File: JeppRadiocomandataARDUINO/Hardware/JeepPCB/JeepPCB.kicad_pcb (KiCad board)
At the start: 2 copper layers, 47.5 x 32.8 mm, 11 parts, among them J1 Conn_01x03_Male

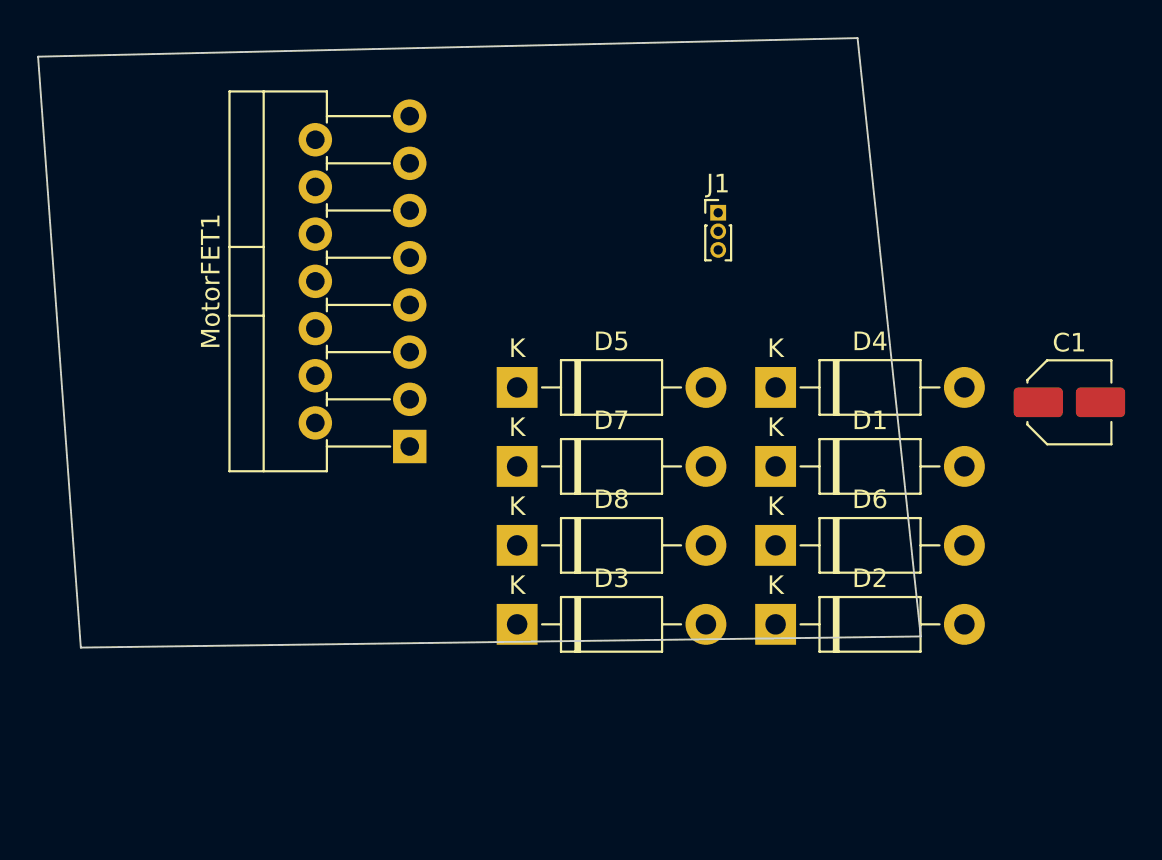
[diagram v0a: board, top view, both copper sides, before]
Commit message: Aggiunta della CPU ATmega328P
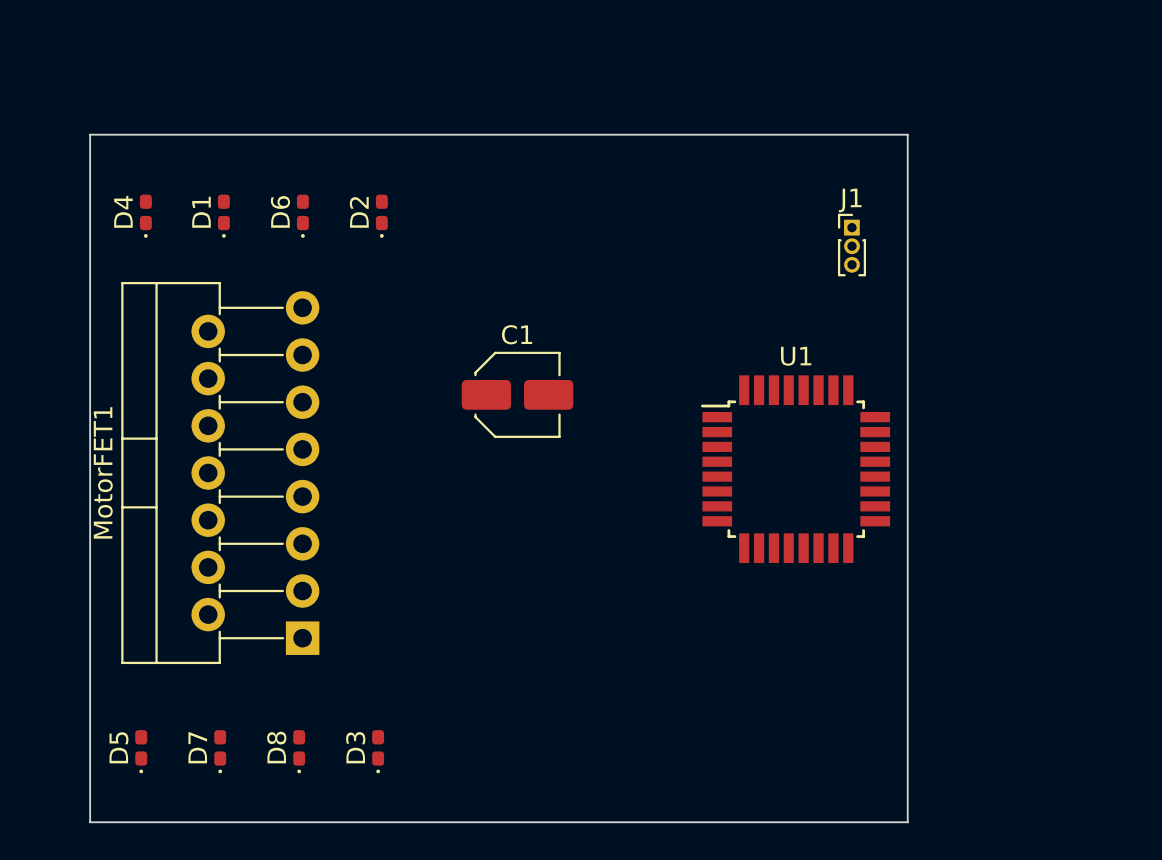
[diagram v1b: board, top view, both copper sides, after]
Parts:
- added U1: ATmega328P-A, Package_QFP:TQFP-32_7x7mm_P0.8mm, F.Cu at (134.0, 77.0)
- D1, D2, D3, D4, D5, D6, D7, D8: footprint Diode_THT:D_DO-41_SOD81_P10.16mm_Horizontal -> Diode_SMD:D_0402_1005Metric_Pad0.77x0.64mm_HandSolder
- J1: value Conn_01x03_Male -> Radio
- moved D4 35.2 mm to (99.0, 63.2), turned to 90 degrees
- moved D1 32.7 mm to (103.2, 63.2), turned to 90 degrees
- moved D6 31.1 mm to (107.5, 63.2), turned to 90 degrees
- moved D2 30.7 mm to (111.7, 63.2), turned to 90 degrees
- moved C1 29.7 mm to (119.0, 73.0)
- moved D5 28.0 mm to (98.8, 92.0), turned to 90 degrees
- moved D7 22.0 mm to (103.0, 92.0), turned to 90 degrees
- moved D8 16.0 mm to (107.2, 92.0), turned to 90 degrees
- moved MotorFET1 11.8 mm to (107.4, 86.1)
- moved D3 10.0 mm to (111.5, 92.0), turned to 90 degrees
- moved J1 7.24 mm to (137.0, 64.0)
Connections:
- J1 pad 1: Net-(J1-Pad1) -> unconnected-(J1-Pad1)
- J1 pad 2: Net-(J1-Pad2) -> unconnected-(J1-Pad2)
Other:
- board size 47.5 x 32.8 mm -> 44 x 37 mm

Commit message: Aggiornamento del PCB
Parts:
- added REG_LIN1: KA78M05_TO252, Package_TO_SOT_SMD:TO-252-2, F.Cu at (114.0, 83.0)
- added C2: 220uF, Capacitor_SMD:C_Elec_4x5.8, F.Cu at (124.0, 78.0)
- added J_BACK1: Screw_Terminal_01x02, TerminalBlock_Phoenix:TerminalBlock_Phoenix_MKDS-1,5-2-5.08_1x02_P5.08mm_Horizontal, F.Cu at (127.5, 59.7)
- added J_FRONT1: Screw_Terminal_01x02, TerminalBlock_Phoenix:TerminalBlock_Phoenix_MKDS-1,5-2-5.08_1x02_P5.08mm_Horizontal, F.Cu at (122.5, 89.3)
- added J_MAIN_POWER1: Screw_Terminal_01x03, TerminalBlock_Phoenix:TerminalBlock_Phoenix_MKDS-1,5-3_1x03_P5.00mm_Horizontal, F.Cu at (137.3, 92.0)
- moved U1 4.00 mm to (134.0, 73.0)
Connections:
- net OUT1 renamed Net-(D1-Pad1)
- net OUT2 renamed Net-(D2-Pad1)
- net OUT3 renamed Net-(D3-Pad1)
- net OUT4 renamed Net-(D4-Pad1)
- J1 pad 1: unconnected-(J1-Pad1) -> Earth
- MotorFET1 pad 10: unconnected-(MotorFET1-Pad10) -> INO_D7
- MotorFET1 pad 11: unconnected-(MotorFET1-Pad11) -> INO_D5
- MotorFET1 pad 12: unconnected-(MotorFET1-Pad12) -> INO_D6
- MotorFET1 pad 5: unconnected-(MotorFET1-Pad5) -> INO_D9
- MotorFET1 pad 6: unconnected-(MotorFET1-Pad6) -> INO_D10
- MotorFET1 pad 7: unconnected-(MotorFET1-Pad7) -> INO_D8
- MotorFET1 pad 9: unconnected-(MotorFET1-Pad9) -> Net-(J_MAIN_POWER1-Pad3)
- U1 pad 21: Net-(U1-Pad21) -> Earth
- U1 pad 3: Net-(U1-Pad21) -> Earth
- U1 pad 5: Net-(U1-Pad21) -> Earth
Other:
- board size 44 x 37 mm -> 48 x 43 mm

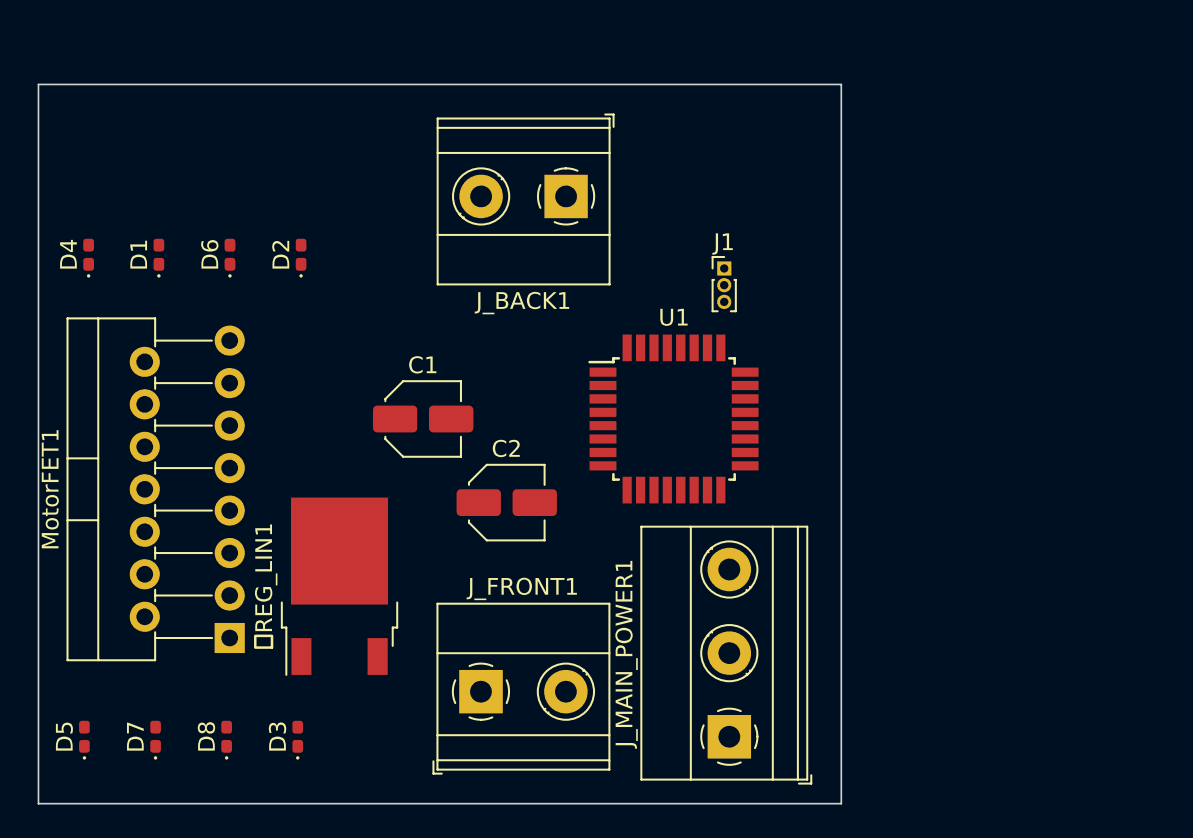
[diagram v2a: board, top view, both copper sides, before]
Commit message: Aggiornamento PCB Jeep
Aggiunta delle connessioni necessarie per il processore
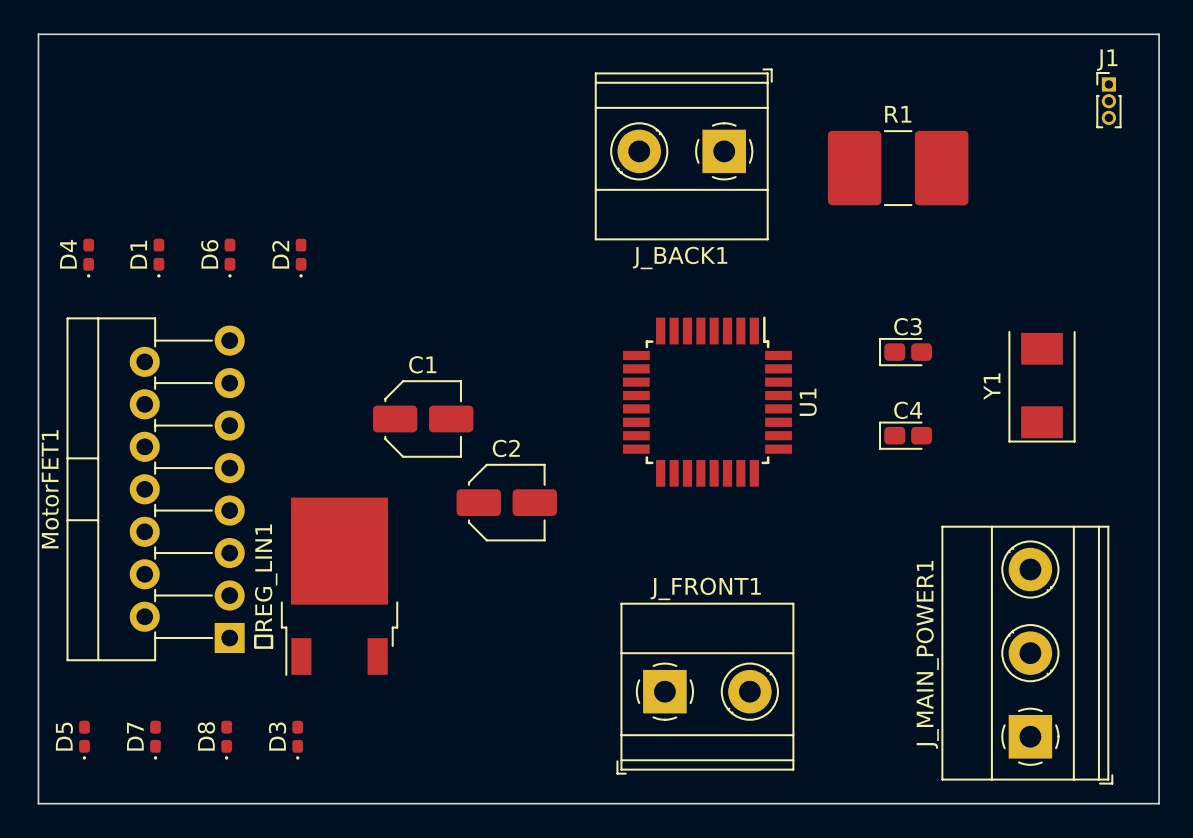
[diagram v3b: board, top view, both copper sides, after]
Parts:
- added C3: 22pF, Capacitor_Tantalum_SMD:CP_EIA-1608-10_AVX-L_Pad1.25x1.05mm_HandSolder, F.Cu at (148.0, 69.0)
- added C4: 22pF, Capacitor_Tantalum_SMD:CP_EIA-1608-10_AVX-L_Pad1.25x1.05mm_HandSolder, F.Cu at (148.0, 74.0)
- added R1: 10K, Resistor_SMD:R_2816_7142Metric_Pad3.20x4.45mm_HandSolder, F.Cu at (147.4, 58.0)
- added Y1: Crystal, Crystal:Crystal_SMD_0603-2Pin_6.0x3.5mm, F.Cu at (156.0, 71.0)
- moved J1 25.5 mm to (160.0, 53.0)
- moved J_MAIN_POWER1 18.0 mm to (155.3, 92.0)
- moved J_FRONT1 11.0 mm to (133.5, 89.3)
- moved J_BACK1 9.83 mm to (137.0, 57.0)
- moved U1 2.24 mm to (136.0, 72.0), turned to -90 degrees
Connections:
- net Net-(C1-Pad1) renamed /5-12V
- REG_LIN1 pad 3: Net-(J_MAIN_POWER1-Pad3) -> VCC
- C2 pad 1: Net-(J_MAIN_POWER1-Pad3) -> VCC
- J1 pad 2: unconnected-(J1-Pad2) -> VCC
- J_MAIN_POWER1 pad 3: Net-(J_MAIN_POWER1-Pad3) -> VCC
- MotorFET1 pad 9: Net-(J_MAIN_POWER1-Pad3) -> VCC
- U1 pad 10: unconnected-(U1-Pad10) -> INO_D6
- U1 pad 11: unconnected-(U1-Pad11) -> INO_D7
- U1 pad 12: unconnected-(U1-Pad12) -> INO_D8
- U1 pad 13: unconnected-(U1-Pad13) -> INO_D9
- U1 pad 14: unconnected-(U1-Pad14) -> INO_D10
- U1 pad 18: unconnected-(U1-Pad18) -> VCC
- U1 pad 20: unconnected-(U1-Pad20) -> VCC
- U1 pad 29: unconnected-(U1-Pad29) -> Net-(R1-Pad2)
- U1 pad 4: Net-(U1-Pad4) -> VCC
- U1 pad 6: Net-(U1-Pad4) -> VCC
- U1 pad 7: unconnected-(U1-Pad7) -> Net-(C3-Pad2)
- U1 pad 8: unconnected-(U1-Pad8) -> Net-(C4-Pad2)
- U1 pad 9: unconnected-(U1-Pad9) -> INO_D5
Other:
- board size 48 x 43 mm -> 67 x 46 mm

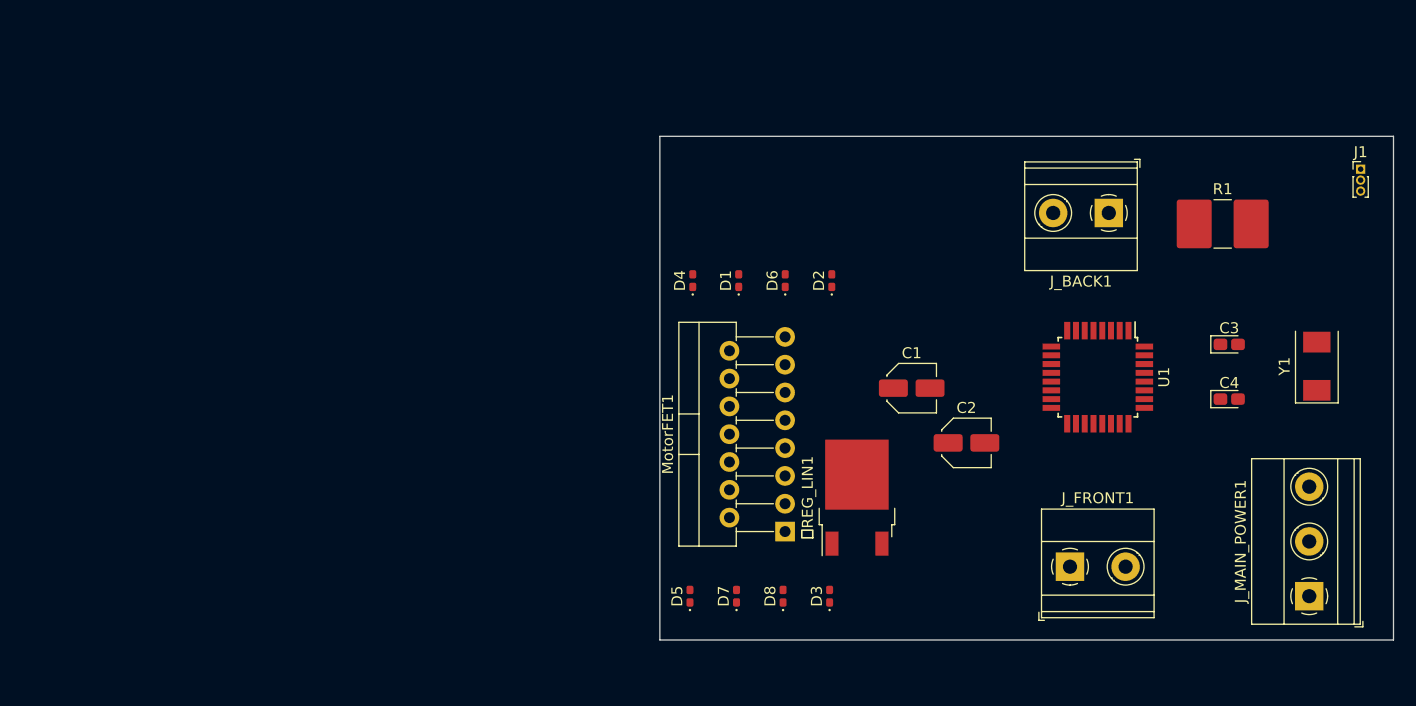
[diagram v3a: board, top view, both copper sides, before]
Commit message: Aggiornamento della resistenza da 10K e posizionamento dei componenti
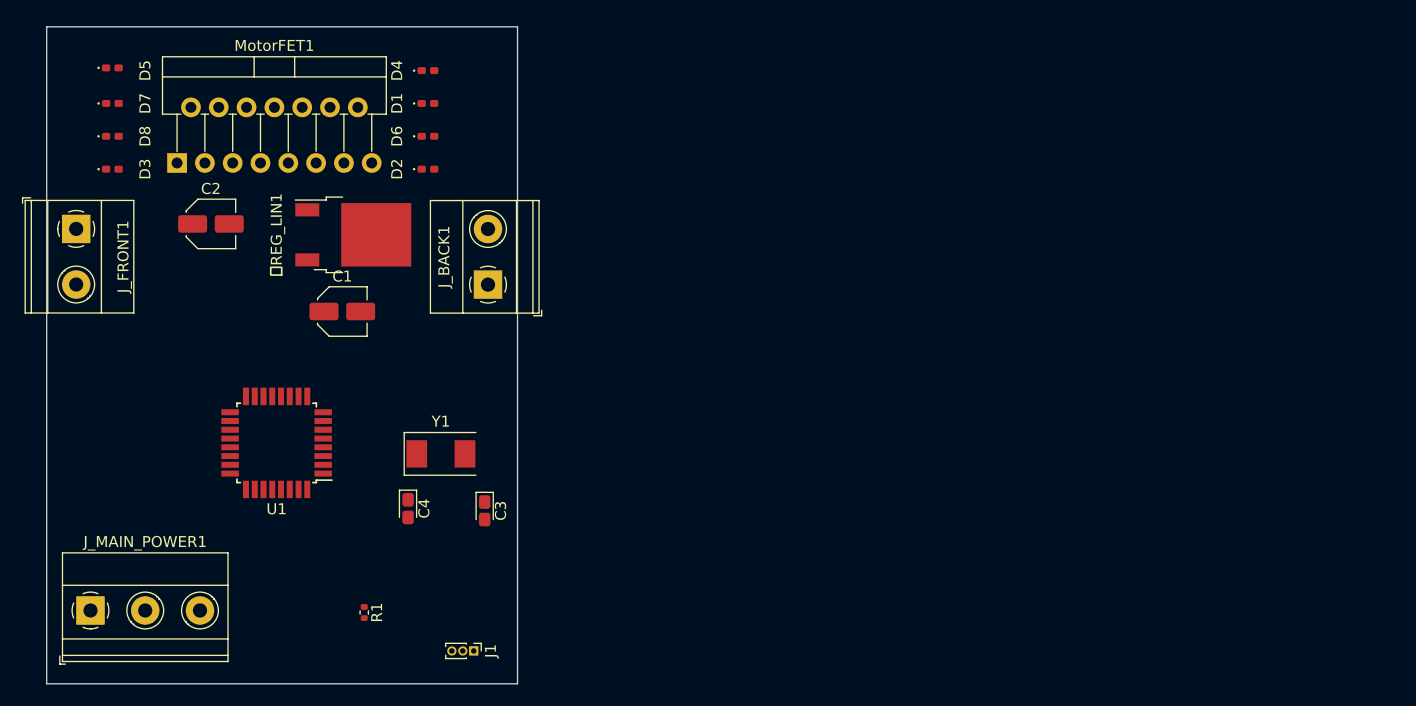
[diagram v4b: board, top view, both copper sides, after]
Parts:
- R1: footprint Resistor_SMD:R_2816_7142Metric_Pad3.20x4.45mm_HandSolder -> Resistor_SMD:R_0402_1005Metric
- moved J_MAIN_POWER1 111.3 mm to (44.0, 93.3), turned to 0 degrees
- moved J_FRONT1 95.9 mm to (42.7, 58.5), turned to -90 degrees
- moved J1 92.2 mm to (79.0, 97.0), turned to -90 degrees
- moved R1 86.1 mm to (69.0, 93.5), turned to -90 degrees
- moved Y1 80.4 mm to (76.0, 79.0), turned to 0 degrees
- moved D3 76.2 mm to (46.0, 53.0), turned to 0 degrees
- moved C4 75.7 mm to (73.0, 84.0), turned to -90 degrees
- moved U1 75.2 mm to (61.0, 78.0), turned to 180 degrees
- moved D8 74.3 mm to (46.0, 50.0), turned to 0 degrees
- moved D7 72.6 mm to (46.0, 47.0), turned to 0 degrees
- moved C2 71.8 mm to (55.0, 58.0)
- moved D5 71.5 mm to (46.0, 43.8), turned to 0 degrees
- moved C3 69.7 mm to (80.0, 84.2), turned to -90 degrees
- moved MotorFET1 64.9 mm to (51.9, 52.4), turned to 0 degrees
- moved J_BACK1 57.1 mm to (80.3, 63.5), turned to 90 degrees
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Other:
- board size 67 x 46 mm -> 43 x 60 mm
